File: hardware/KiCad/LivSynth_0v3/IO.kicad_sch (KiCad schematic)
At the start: 95 parts, among them J1 PJ398SM, J13 Jumper, J14 Jumper, J2 PJ398SM, J20 IDC, J3 PJ398SM, J4 IDC, Q6 2N3904, Q7 2N3904, SW6 SW_Push, U10 PCA9685PW, U11 PCA9685PW, U13 74HC165, U14 74HC165, U3 LM386

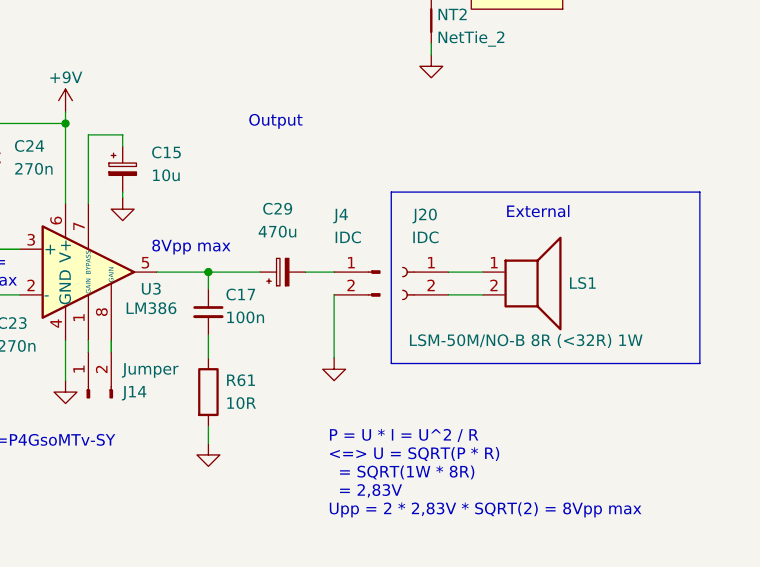
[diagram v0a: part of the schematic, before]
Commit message: Add another LFO cap for easier modding please MCU connectors to the backside Relocate reset button KiCad 7.0.1
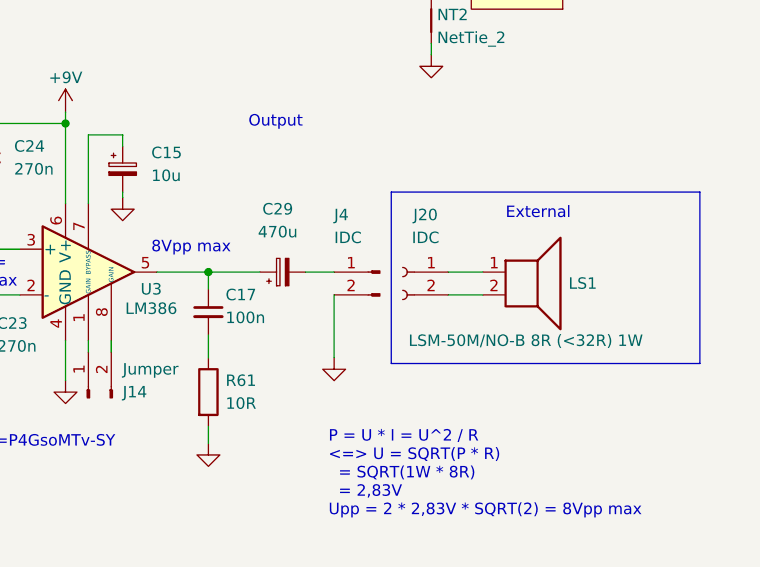
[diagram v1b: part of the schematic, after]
